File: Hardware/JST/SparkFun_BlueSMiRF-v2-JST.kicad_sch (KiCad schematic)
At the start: 38 parts, among them J1 JST_Locking_6, Q1 BSS138, Q2 BSS138, SW1 SMD_4.6x2.8mm_h2.5mm, U1 ESP32-PICO-V3-02, U2 AP2112K-3.3

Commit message: Update/Add Page Details
Add project details
- Company
- Project Name
- Designer
- Revision #
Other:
- company: (none) -> SparkFun Electronics
- title: SparkFun BlueSMiRF v2 Headers -> SparkFun BlueSMiRF v2 JST
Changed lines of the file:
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@@
 	(paper "USLetter")
 	(title_block
-		(title "SparkFun BlueSMiRF v2 Headers")
-		(date "2023-07-29")
-		(rev "v11")
-		(comment 1 "Designed by: N. Seidle")
+		(title "SparkFun BlueSMiRF v2 JST")
+		(date "2025-12-04")
+		(rev "v10")
+		(company "SparkFun Electronics")
+		(comment 1 "Designed by: Wes Furuya")
 	)
 	(text "Max input voltage: 6V"

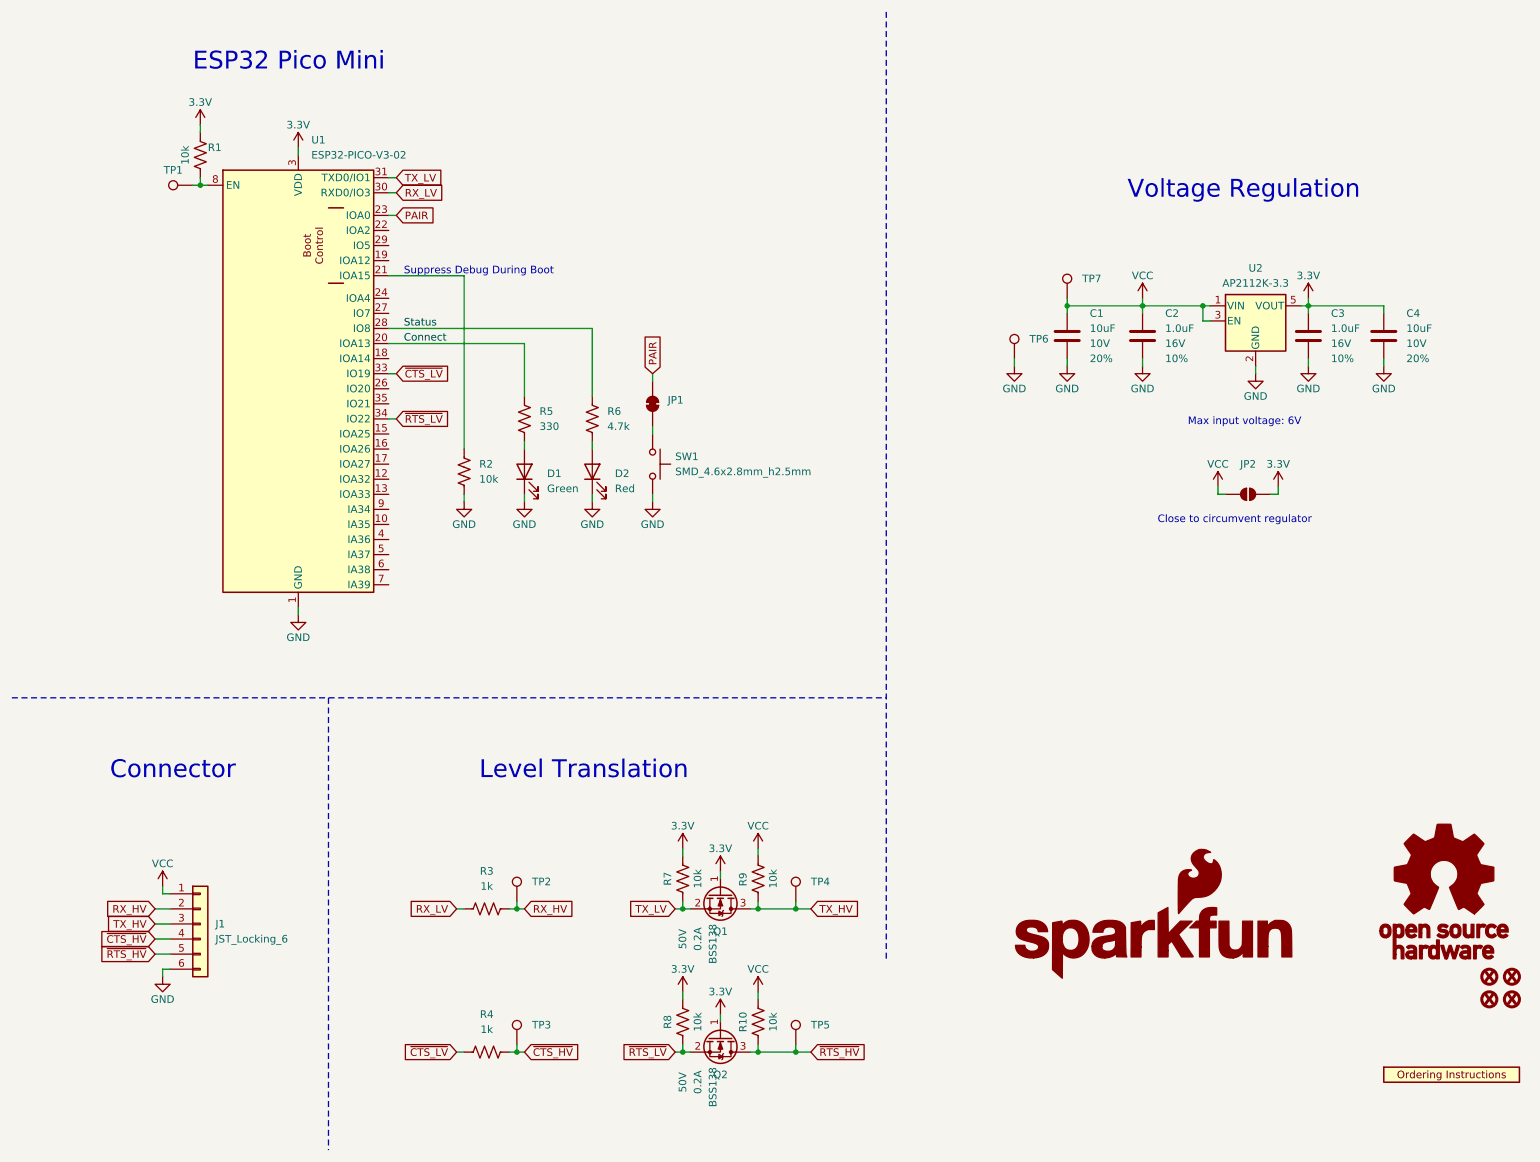
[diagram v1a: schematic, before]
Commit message: Design Update
Update symbols and footprints based on latest SparkFun library
Extended board length to line up with grid layout: 1.5" -> 1.6"
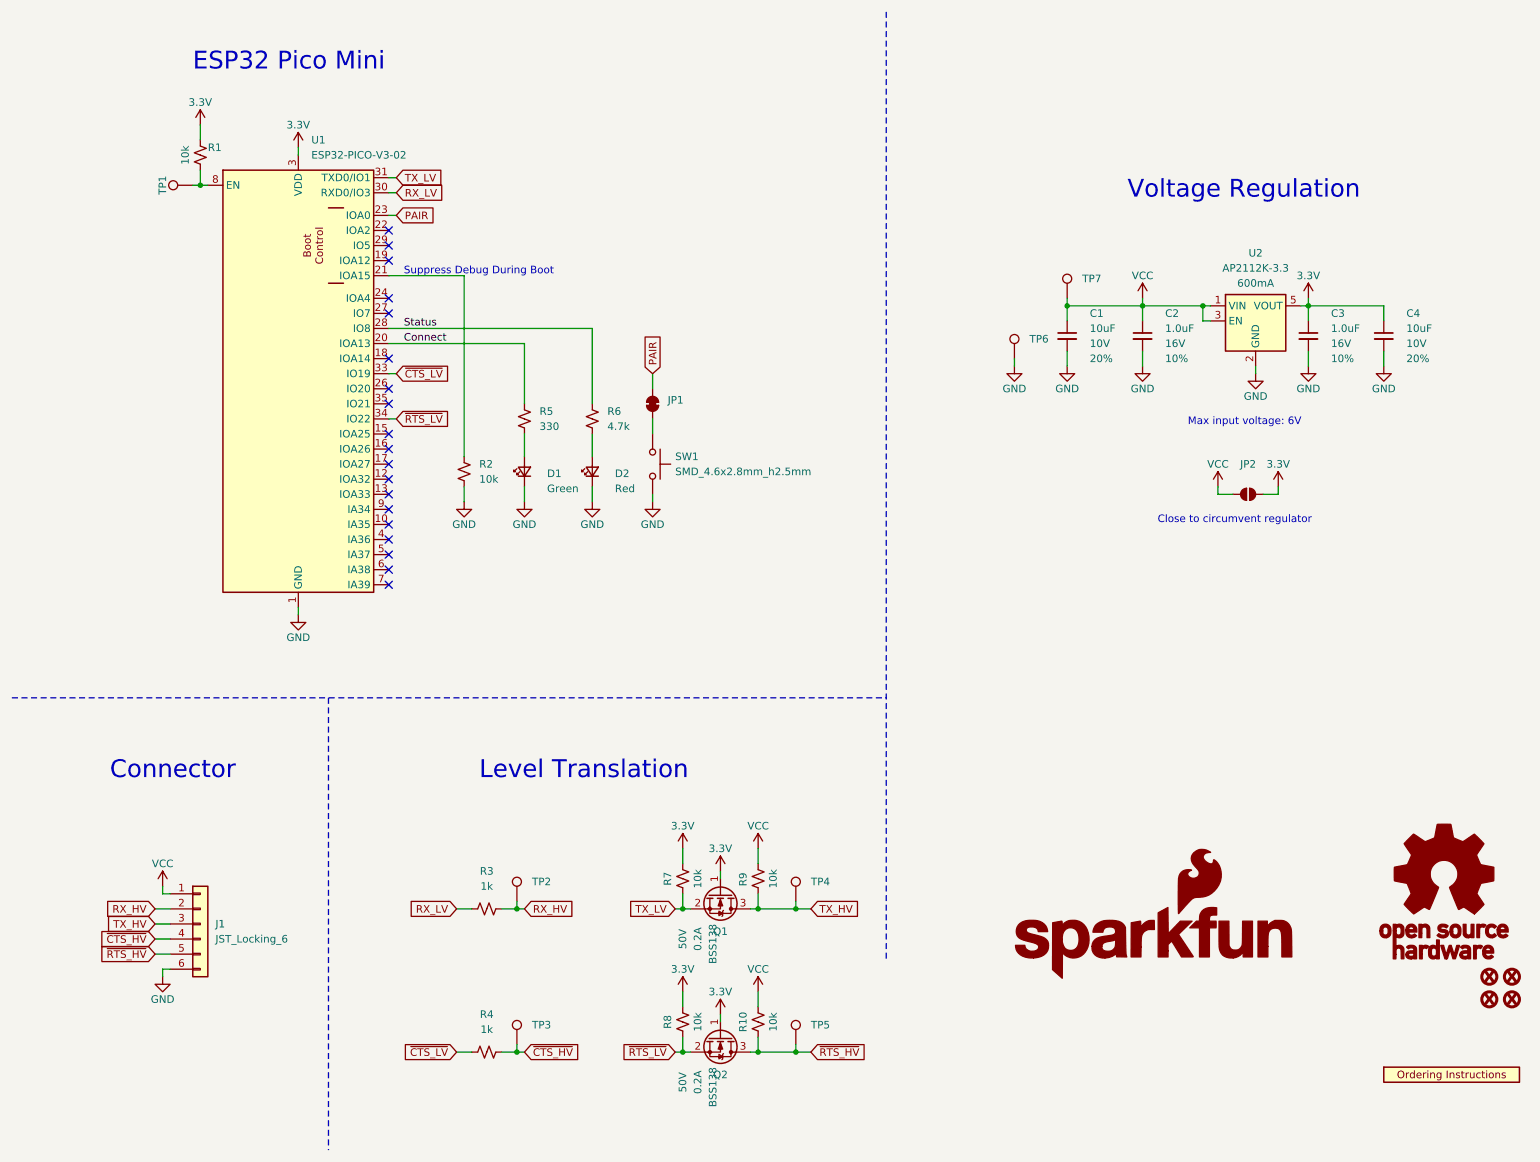
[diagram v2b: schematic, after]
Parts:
- J1: footprint SparkFun-Connector:JST_SMD_1.25mm-6_Locking -> SparkFun-Connector:JST_1x06_P1.25mm_Locking_Horizontal_SMD; symbol SparkFun-Connector:Conn_01x06_JST_1.25mm_Locking -> SparkFun-Connector:Conn_01x06_JST_P1.25mm_Locking_Horizontal_SMD
- TP1: footprint SparkFun-Connector:1x01 -> SparkFun-Connector:1x01_P2.54mm
- U2: IMax (none) -> 600mA
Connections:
- net 3.3V: now also R1.2, R7.1, R8.1; no longer R1.1, R7.2, R8.2
- net Connect: now also R5.2; no longer R5.1
- net GND: now also R2.2; no longer R2.1
- net RX_HV: now also R3.1; no longer R3.2
- net RX_LV: now also R3.2; no longer R3.1
- net Status: now also R6.2; no longer R6.1
- net TX_HV: now also R9.2; no longer R9.1
- net TX_LV: now also R7.2; no longer R7.1
- net VCC: now also R10.1, R9.1; no longer R10.2, R9.2
- net ~{CTS_HV}: now also R4.1; no longer R4.2
- net ~{CTS_LV}: now also R4.2; no longer R4.1
- net ~{RTS_HV}: now also R10.2; no longer R10.1
- net ~{RTS_LV}: now also R8.2; no longer R8.1
- net at D1.2 (A): now also R5.1; no longer R5.2
- net at U1.21 (IOA15): now also R2.1; no longer R2.2
- net at TP1.1, U1.8 (EN): now also R1.1; no longer R1.2
- net at D2.2 (A): now also R6.1; no longer R6.2
- no-connect marks 0 -> 19
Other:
- moved on the sheet: D1, D2
